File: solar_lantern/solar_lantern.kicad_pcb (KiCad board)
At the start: 2 copper layers, 153 x 133 mm, 53 parts, among them J1 PV, J2 AVR-ISP-6, Q1 RU20P7C, Q2 RU20P7C, Q3 RU20P7C, SW1 SW_Push, U1 CN3791, U2 ATtiny441-SS, U3 MCP1664

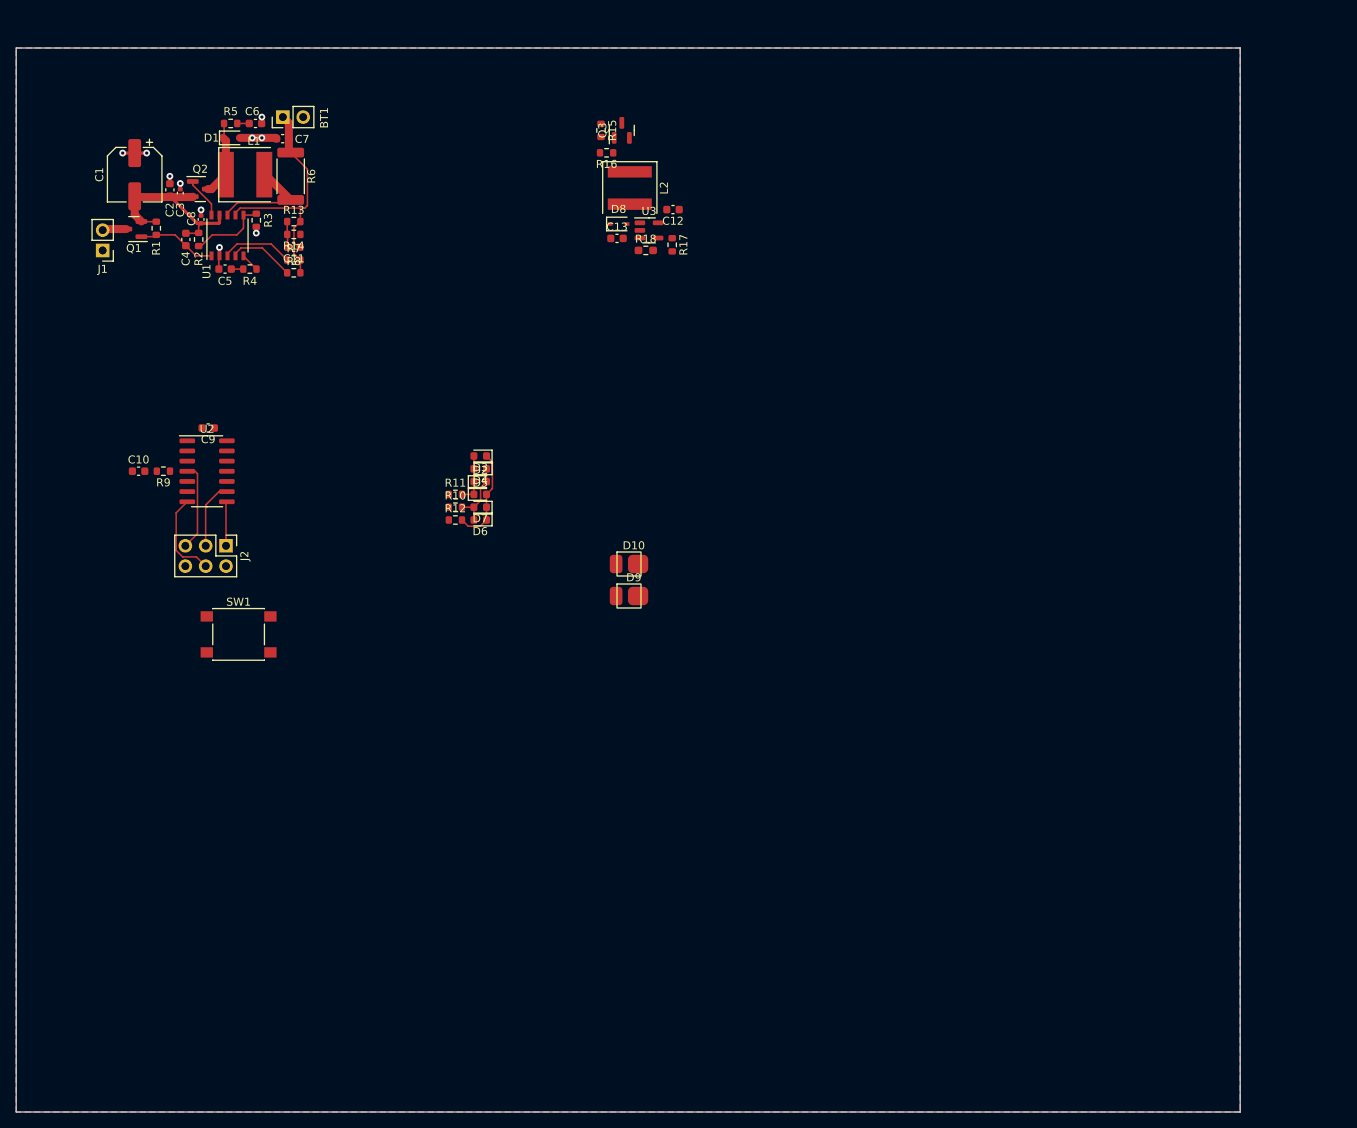
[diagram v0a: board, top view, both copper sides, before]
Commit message: Make board smaller, Fix bad cap orientation, Add a diode to reduce quescient current
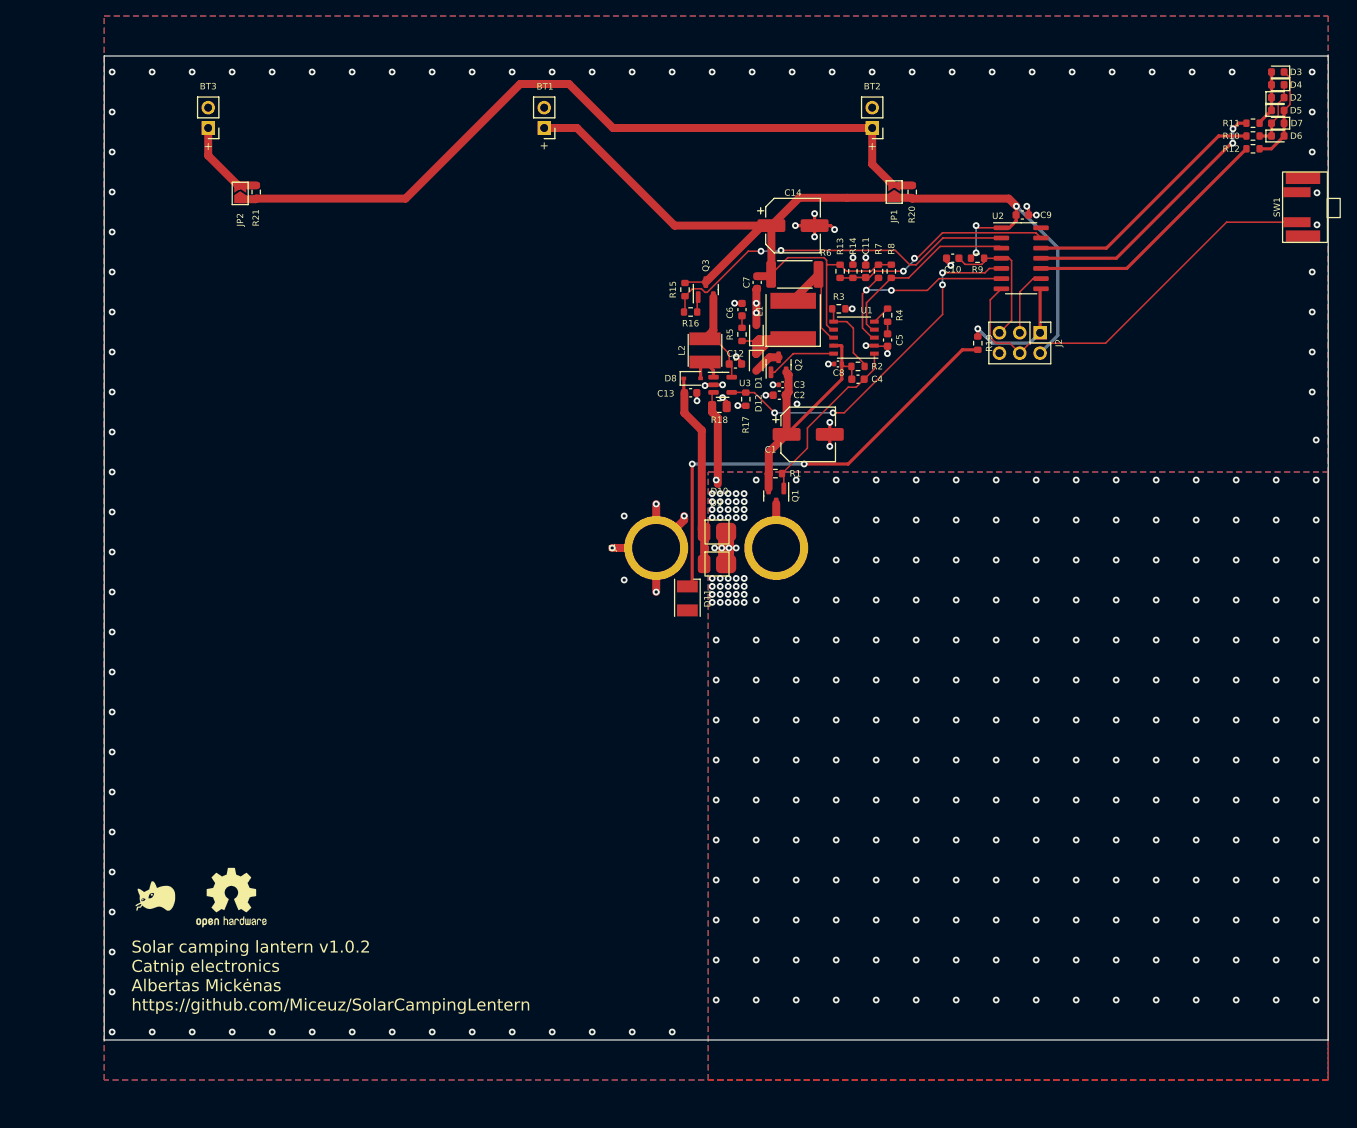
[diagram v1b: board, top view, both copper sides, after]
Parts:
- added BT2: Battery_Cell, Connector_PinHeader_2.54mm:PinHeader_1x02_P2.54mm_Vertical, F.Cu at (146.0, 31.0)
- added BT3: Battery_Cell, Connector_PinHeader_2.54mm:PinHeader_1x02_P2.54mm_Vertical, F.Cu at (63.0, 31.0)
- added C14: 100u, Capacitor_SMD:CP_Elec_6.3x5.4_Nichicon, F.Cu at (136.1, 43.2)
- added D11: RED LED, LED_SMD:LED_PLCC-2, F.Cu at (122.9, 89.8)
- added D12: D_Schottky, Diode_SMD:D_SOD-323, F.Cu at (131.5, 60.3)
- added G***: LOGO, miceuz-lib:catnip, F.Cu at (56.4, 127.0)
- added JP1: SolderJumper_2_Open, Jumper:SolderJumper-2_P1.3mm_Open_TrianglePad1.0x1.5mm, F.Cu at (148.8, 39.0)
- added JP2: SolderJumper_2_Open, Jumper:SolderJumper-2_P1.3mm_Open_TrianglePad1.0x1.5mm, F.Cu at (67.0, 39.2)
- added R19: 100, Resistor_SMD:R_0603_1608Metric, F.Cu at (159.2, 57.9)
- added R20: 43, Resistor_SMD:R_0603_1608Metric, F.Cu at (151.0, 39.0)
- added R21: 43, Resistor_SMD:R_0603_1608Metric, F.Cu at (69.0, 39.0)
- added REF**: OSHW-Logo2_9.8x8mm_SilkScreen, Symbol:OSHW-Logo2_9.8x8mm_SilkScreen, F.Cu at (65.9, 127.2)
- C1: value 10u -> 100u
- L2: value 47u -> 4u7; footprint Inductor_SMD:L_Coilcraft_XAL60xx_6.36x6.56mm -> Inductor_SMD:L_Taiyo-Yuden_MD-4040
- R10, R11, R12: value R -> 1k
- R18: footprint Resistor_SMD:R_0603_1608Metric_Pad0.98x0.95mm_HandSolder -> Resistor_SMD:R_0805_2012Metric
- R2: value R -> 75k
- R3: value R -> 22k
- R5: value R -> 120
- R7, R8: value R -> 1M
- moved SW1 146.2 mm to (202.9, 40.9), turned to 90 degrees
- moved D2 110.7 mm to (196.7, 27.2)
- moved D3 110.7 mm to (196.7, 24.0)
- moved D5 110.7 mm to (196.7, 28.8)
- moved D6 110.7 mm to (196.7, 32.0), turned to 0 degrees
- moved D7 110.7 mm to (196.7, 30.4)
- moved D4 110.7 mm to (196.7, 25.6)
- moved R10 110.0 mm to (193.6, 32.0)
- moved R11 110.0 mm to (193.6, 30.4)
- moved R12 110.0 mm to (193.6, 33.6)
- moved C10 105.2 mm to (156.1, 47.3)
- moved U2 105.2 mm to (164.6, 47.3)
- moved C9 105.2 mm to (164.8, 41.9)
- moved J2 105.2 mm to (167.0, 56.6)
- moved R9 105.2 mm to (159.2, 47.3)
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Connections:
- C1 pad 1: GND -> /Solar charger/PV_VOLTAGE
- C1 pad 2: /Solar charger/PV_VOLTAGE -> GND
- D6 pad 1: Net-(D3-Pad1) -> Net-(D2-Pad2)
- D6 pad 2: Net-(D2-Pad2) -> Net-(D3-Pad1)
- Q2 pad 3: /Solar charger/SW_NODE -> Net-(Q2-Pad3)
- U2 pad 2: /~{DONE} -> /~{LED_EN}
- U2 pad 3: /~{LED_EN} -> /~{DONE}
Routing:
- net +BATT: track 30.8 -> 146.7 mm, vias 0 -> 3
- net Net-(BT2-Pad1): track 0.00 -> 96.9 mm
- net Net-(D11-Pad1): track 0.00 -> 57.2 mm, vias 0 -> 2
- net /~{LED_EN}: track 0.00 -> 46.5 mm, vias 0 -> 2
- net /LED_PWM: track 0.00 -> 45.3 mm, vias 0 -> 4
- net GND: track 14.3 -> 57.1 mm, vias 10 -> 109
- net /MOSI: track 11.2 -> 52.6 mm
- net /CHARLIE_2: track 0.00 -> 33.7 mm, vias 0 -> 2
- net /CHARLIE_3: track 0.00 -> 31.9 mm
- net /CHARLIE_1: track 0.00 -> 31.5 mm
- net /BATT_VOLTAGE: track 3.22 -> 27.7 mm, vias 0 -> 2
- net /VCC_LED: track 0.00 -> 24.3 mm
- net /~{CHARGING}: track 9.08 -> 26.6 mm, vias 0 -> 2
- net /LED_FB: track 0.00 -> 15.6 mm, vias 0 -> 262
- net /~{DONE}: track 8.33 -> 23.8 mm
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- added copper zone on B.Cu, net /LED_FB
- added copper zone on F.Cu, net /LED_FB
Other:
- board size 153 x 133 mm -> 153 x 123 mm
- board text added: "+"
- board text added: "Battery cell dimensions: 38x14x7.7"
- board text added: "Solar camping lantern v1.0.2 Catnip electronics Albertas Mickėnas https://github.com/Miceuz/SolarCampingLentern"

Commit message: Fix PCB thickness, add some measirements to PCB
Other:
- board text added: "Solar cell size: 165x135mm"
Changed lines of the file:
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@@
 (kicad_pcb (version 20211014) (generator pcbnew)
   (general
-    (thickness 1.6)
+    (thickness 0.8)
   )
   (paper "A4")
@@
       (layer "F.Mask" (type "Top Solder Mask") (color "White") (thickness 0.01))
       (layer "F.Cu" (type "copper") (thickness 0.035))
-      (layer "dielectric 1" (type "core") (thickness 1.51) (material "FR4") (epsilon_r 4.5) (loss_tangent 0.02))
+      (layer "dielectric 1" (type "core") (thickness 0.71) (material "FR4") (epsilon_r 4.5) (loss_tangent 0.02))
       (layer "B.Cu" (type "copper") (thickness 0.035))
       (layer "B.Mask" (type "Bottom Solder Mask") (color "White") (thickness 0.01))
@@
     (effects (font (size 1 1) (thickness 0.15)))
   )
+  (gr_text "Solar cell size: 165x135mm" (at 107.8 167.1) (layer "Cmts.User")
+    (effects (font (size 1 1) (thickness 0.15)))
+  )
   (dimension (type aligned) (layer "Cmts.User")
     (pts (xy 50 22) (xy 50 145))
@@
       (effects (font (size 1 1) (thickness 0.15)))
     )
+    (format (units 2) (units_format 1) (precision 1))
+    (style (thickness 0.1) (arrow_length 1.27) (text_position_mode 0) (extension_height 0.58642) (extension_offset 0.5) keep_text_aligned)
+  )
+  (dimension (type aligned) (layer "Cmts.User")
+    (pts (xy 203 22) (xy 202.9 41))
+    (height -4.199941)
+    (gr_text "19,0 mm" (at 205.999899 31.516052 89.69844605) (layer "Cmts.User")
+      (effects (font (size 1 1) (thickness 0.15)))
+    )

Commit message: Add CERN-OHL_S licence
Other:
- board text added: "This source is distributed WITHOUT ANY EXPRESS OR IMPLIED WARRANTY, INCLUDING OF MERCHANTABILITY, SATISFACTORY QUALITY AND FITNESS FOR A PARTICULAR PURPOSE. Please see the CERN-OHL-S v2 for applicable conditions. Source location: https://example_url As per CERN-OHL-S v2 section 4, should You produce hardware based on this source, You must where practicable maintain the Source Location visible on 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"
